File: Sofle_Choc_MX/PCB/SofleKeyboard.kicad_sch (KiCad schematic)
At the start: 75 parts, among them J1 Pimaroni Trackball, J2 4PIN, J3 OLED, SW1 SW_PUSH_LED, SW10 SW_PUSH_LED, SW11 SW_PUSH_LED, SW12 SW_PUSH_LED, SW13 SW_PUSH_LED, SW14 SW_PUSH_LED, SW15 SW_PUSH_LED, SW16 SW_PUSH_LED, SW17 SW_PUSH_LED, SW18 SW_PUSH_LED, SW19 SW_PUSH_LED, SW2 SW_PUSH_LED, SW20 SW_PUSH_LED, SW21 SW_PUSH_LED, SW22 SW_PUSH_LED, SW23 SW_PUSH_LED, SW24 SW_PUSH_LED, SW25 Rotary_Encoder_Switch, SW26 SW_PUSH_LED, SW27 SW_PUSH_LED, SW28 SW_PUSH_LED, SW29 SW_PUSH_LED, SW3 SW_PUSH_LED, SW30 SW_PUSH_LED, SW4 SW_PUSH_LED, SW5 SW_PUSH_LED, SW6 SW_PUSH_LED, SW7 SW_PUSH_LED, SW8 SW_PUSH_LED, SW9 SW_PUSH_LED, U1 ProMicro_Choc_MX

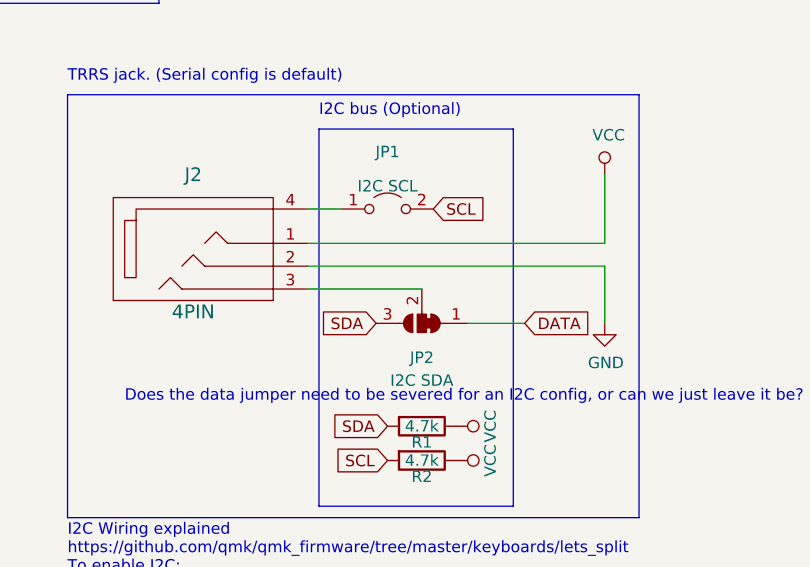
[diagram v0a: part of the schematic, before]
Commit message: Library cleanup and consolidation
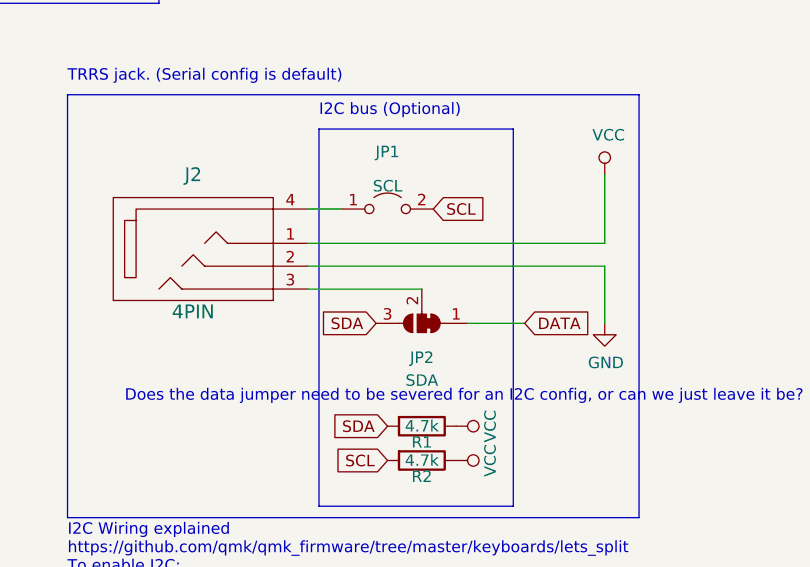
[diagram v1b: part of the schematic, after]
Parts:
- D1, D10, D11, D12, D13, D14, D15, D16, D17, D18, D19, D2, D20, D21, D22, D23, D24, D25, D26, D27, D28, D29, D3, D30, D4, D5, D6, D7, D8, D9: footprint SofleChoc:D_SOD-123_DO-35_Hybrid_DoubleSided -> SofleChocMX:D_SOD-123_DO-35_Hybrid_DoubleSided
- J1: footprint SofleChoc:pimoroni_trackball -> SofleChocMX:pimoroni_trackball
- J2: footprint SofleChoc:MJ-4PP-9_Choc_MX -> SofleChocMX:MJ-4PP-9_Choc_MX
- J3: footprint SofleChoc:OLED_4Pin_Choc_MX -> SofleChocMX:OLED_4Pin_Choc_MX
- JP1: value I2C SCL -> SCL
- JP2: value I2C SDA -> SDA
- R1, R2: footprint SofleChoc:R_I2C_bus -> SofleChocMX:R_I2C_bus
- SW1, SW10, SW11, SW12, SW13, SW14, SW15, SW16, SW17, SW18, SW19, SW2, SW20, SW21, SW22, SW23, SW24, SW26, SW27, SW28, SW29, SW3, SW30, SW4, SW5, SW6, SW7, SW8, SW9: footprint SofleChoc:Choc_MX_Hotswap_SK6812MiniE -> SofleChocMX:Choc_MX_Hotswap_SK6812MiniE
- SW25: footprint SofleKeyboard-footprint:RotaryEncoder_Alps_EC11E-Switch_Vertical_H20mm-keebio_modified -> SofleChocMX:RotaryEncoder_Alps_EC11E-Switch_Vertical_H20mm-keebio_modified
- TH1, TH2: footprint SofleKeyboard-footprint:M2_HOLE_PCB -> SofleChocMX:HOLE_M2_TH
- TH3, TH4, TH5, TH6, TH7: footprint SofleKeyboard-footprint:HOLE_M2_TH -> SofleChocMX:HOLE_M2_TH
- U1: footprint SofleChoc:ProMicro_Choc_MX -> SofleChocMX:ProMicro_Choc_MX

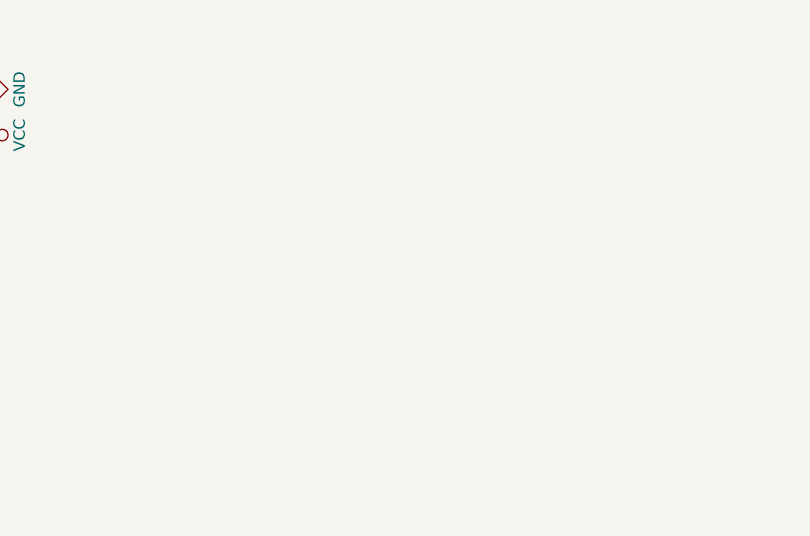
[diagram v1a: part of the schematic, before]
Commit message: Converted i2c jumper pads to through hole and moved diodes
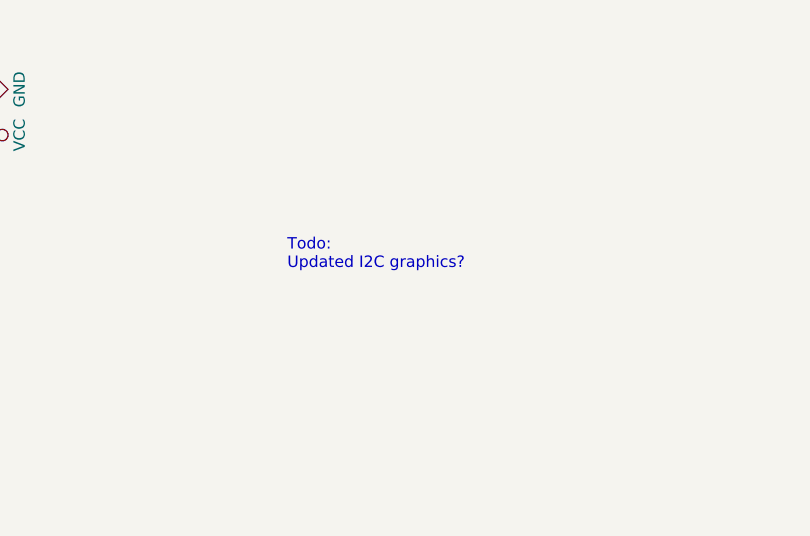
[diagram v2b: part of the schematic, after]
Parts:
- JP1: footprint Jumper:SolderJumper-2_P1.3mm_Open_RoundedPad1.0x1.5mm -> SofleChocMX:PinHeader_1x02_P2.54mm_jumper
- JP2: footprint Jumper:SolderJumper-3_P1.3mm_Bridged12_RoundedPad1.0x1.5mm_NumberLabels -> SofleChocMX:PinHeader_1x03_P2.54mm_jumper
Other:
- note added: "Todo: Updated I2C graphics?"
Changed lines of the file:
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@@
     (effects (font (size 1.27 1.27)) (justify left bottom))
   )
+  (text "Todo:\nUpdated I2C graphics?" (at 102.1466 44.269 0)
+    (effects (font (size 1.27 1.27)) (justify left bottom))
+  )
   (global_label "row3" (shape input) (at 27.94 46.99 180)
     (effects (font (size 1.27 1.27)) (justify right))
@@
       (effects (font (size 1.27 1.27)))
     )
-    (property "Footprint" "Jumper:SolderJumper-3_P1.3mm_Bridged12_RoundedPad1.0x1.5mm_NumberLabels" (at 96.52 125.73 0)
+    (property "Footprint" "SofleChocMX:PinHeader_1x03_P2.54mm_jumper" (at 96.52 125.73 0)
       (effects (font (size 1.27 1.27)) hide)
     )
@@
       (effects (font (size 1.27 1.27)))
     )
-    (property "Footprint" "Jumper:SolderJumper-2_P1.3mm_Open_RoundedPad1.0x1.5mm" (at 76.2 101.6 0)
+    (property "Footprint" "SofleChocMX:PinHeader_1x02_P2.54mm_jumper" (at 76.2 101.6 0)
       (effects (font (size 1.27 1.27)) hide)
     )
